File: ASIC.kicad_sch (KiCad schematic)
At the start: 74 parts, among them U12 TLV75512PDQNR, U14 TLV75512PDQNR, U15 TLV75512PDQNR, U3 TLV75512PDQNR, U8 SN74AXC4T774, Y2 50MHz

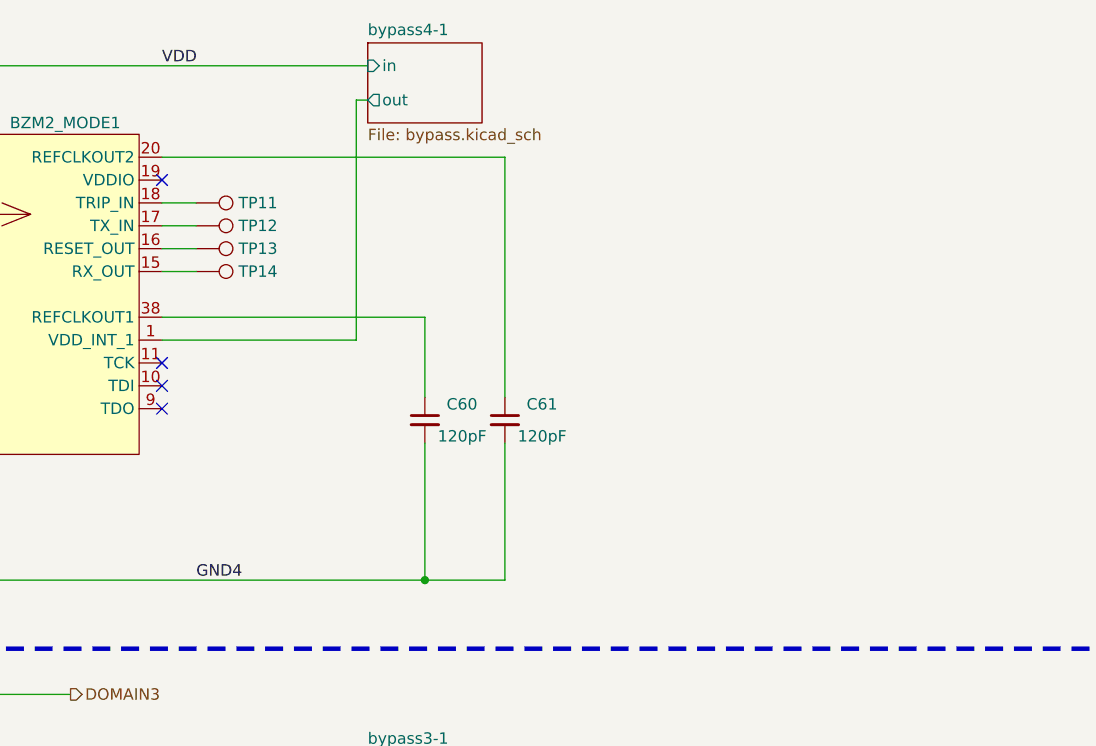
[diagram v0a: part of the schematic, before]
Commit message: added pull resistors for #1
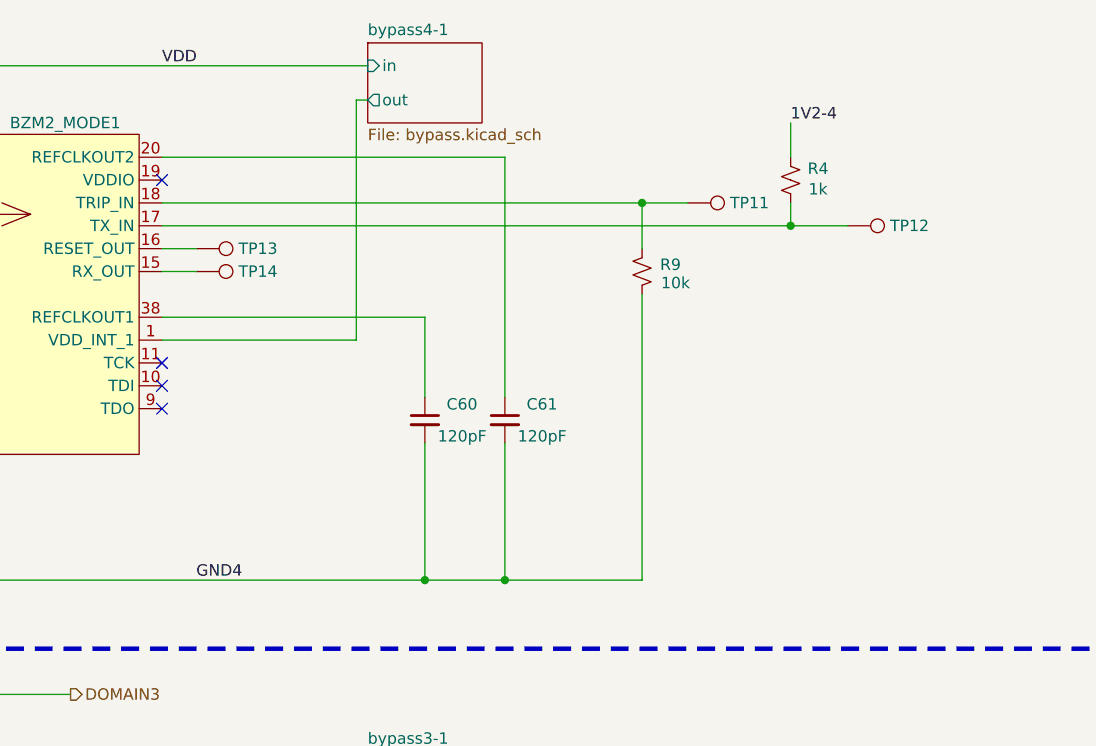
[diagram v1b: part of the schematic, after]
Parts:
- added R4: 1k, Resistor_SMD:R_0402_1005Metric, symbol Device:R_Small_US
- added R9: 10k, Resistor_SMD:R_0402_1005Metric, symbol Device:R_Small_US
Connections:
- net 1V2-4: now also R4.1
- net DOMAIN3: now also R9.2
- net at A4.17 (TX_IN), TP12.1: now also R4.2
- net at A4.18 (TRIP_IN), TP11.1: now also R9.1
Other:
- moved on the sheet: TP11, TP12

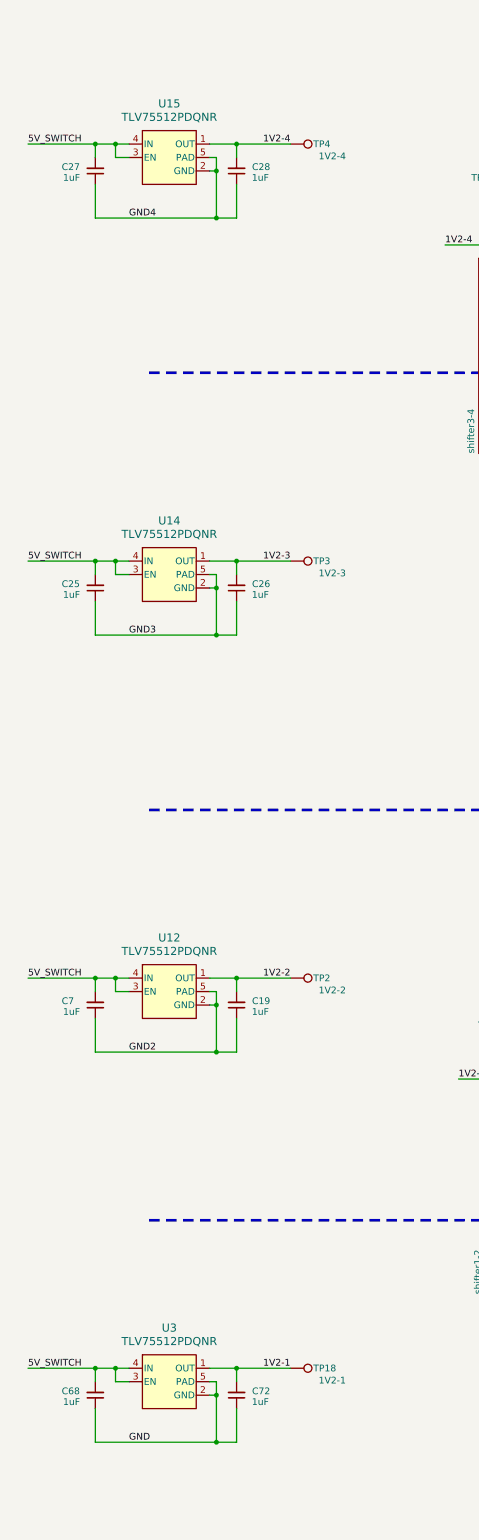
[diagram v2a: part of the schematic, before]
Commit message: change IO voltage LDOs to bigger packages for #6
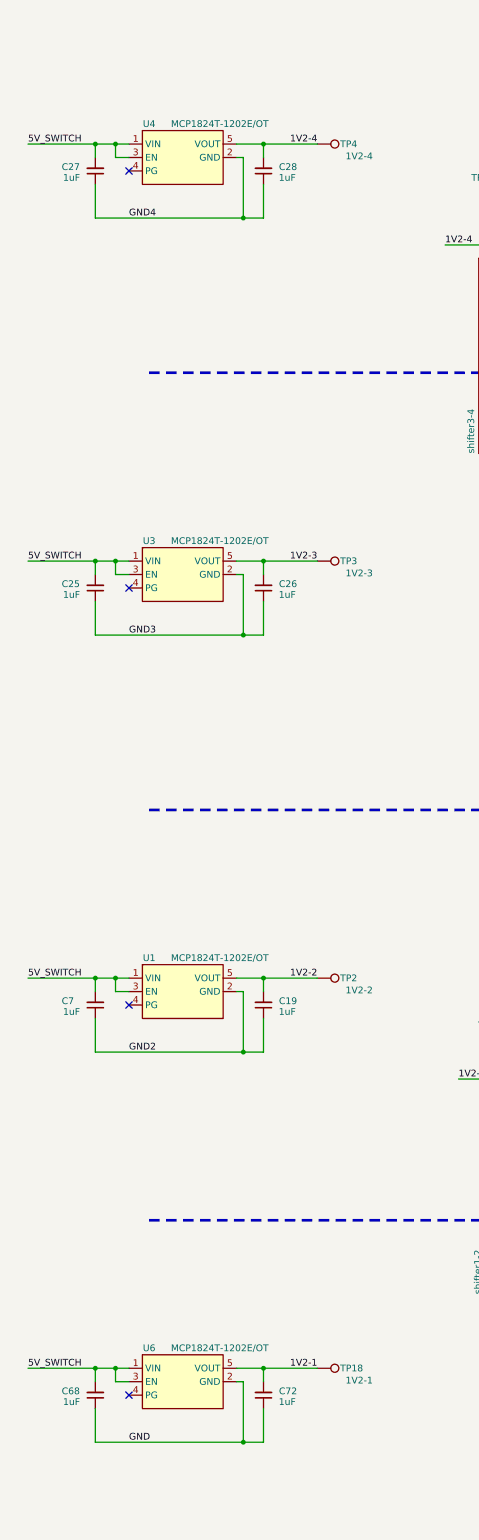
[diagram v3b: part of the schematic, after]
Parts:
- removed U12, U14, U15, U3: TLV75512PDQNR, bitaxe:DQN0004A, symbol bitaxe:TLV75512PDQNR
- added U1, U3, U4, U6: MCP1824T-1202E/OT, Package_TO_SOT_SMD:SOT-23-5, symbol bitaxe:MCP1824
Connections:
- net 1V2-1: now also U6.5 (VOUT)
- net 1V2-2: now also U1.5 (VOUT)
- net 1V2-3: now also U3.5 (VOUT)
- net 1V2-4: now also U4.5 (VOUT)
- net 5V_SWITCH: now also U1.1 (VIN), U1.3 (EN), U3.1 (VIN), U3.3 (EN), U4.1 (VIN), U4.3 (EN), U6.1 (VIN), U6.3 (EN)
- net DOMAIN1: now also U1.2 (GND)
- net DOMAIN2: now also U3.2 (GND)
- net DOMAIN3: now also U4.2 (GND)
- net GND: now also U6.2 (GND)
- no-connect marks 26 -> 30
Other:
- moved on the sheet: C19, C26, C28, C72, TP18, TP2, TP3, TP4

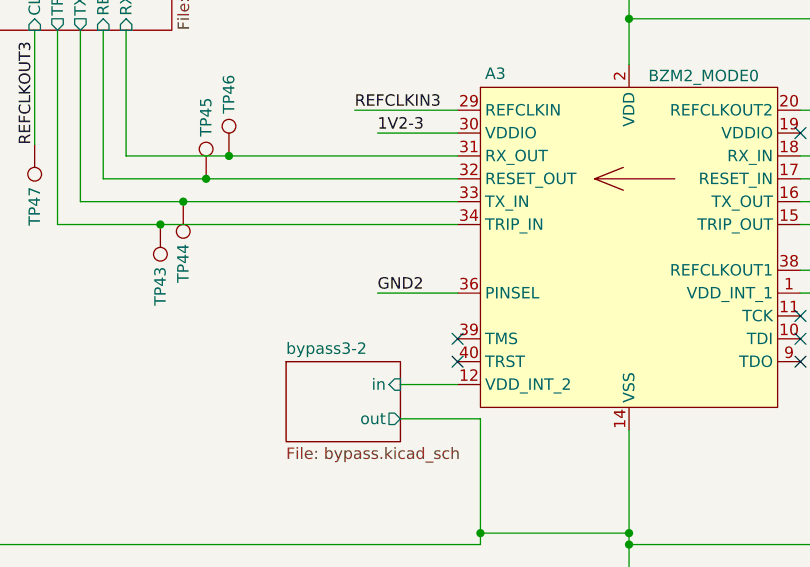
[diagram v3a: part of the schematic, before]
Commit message: fix pinsel connection on ASIC 3 for #7
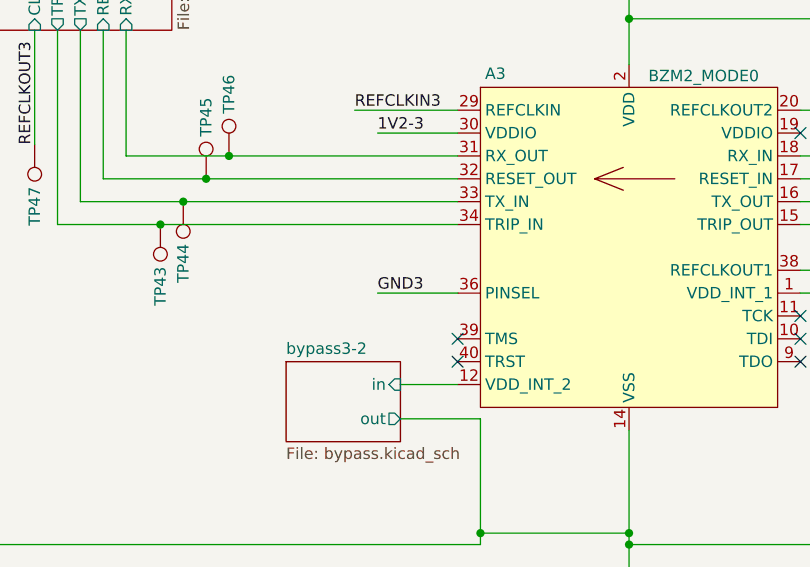
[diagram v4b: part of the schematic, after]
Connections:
- net DOMAIN1: no longer A3.36 (PINSEL)
- net DOMAIN2: now also A3.36 (PINSEL)
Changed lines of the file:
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@@
 		)
 	)
-	(label "GND2"
+	(label "GND3"
 		(at 259.08 171.45 0)
 		(effects
